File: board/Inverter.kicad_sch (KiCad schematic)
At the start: 19 parts, among them IC2 TLI4971A075T5UE0001XUMA1, Q1 IGC033S101, Q10 IGC033S101, Q11 IGC033S101, Q12 IGC033S101, Q2 IGC033S101, Q3 IGC033S101, Q4 IGC033S101, Q5 IGC033S101, Q6 IGC033S101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

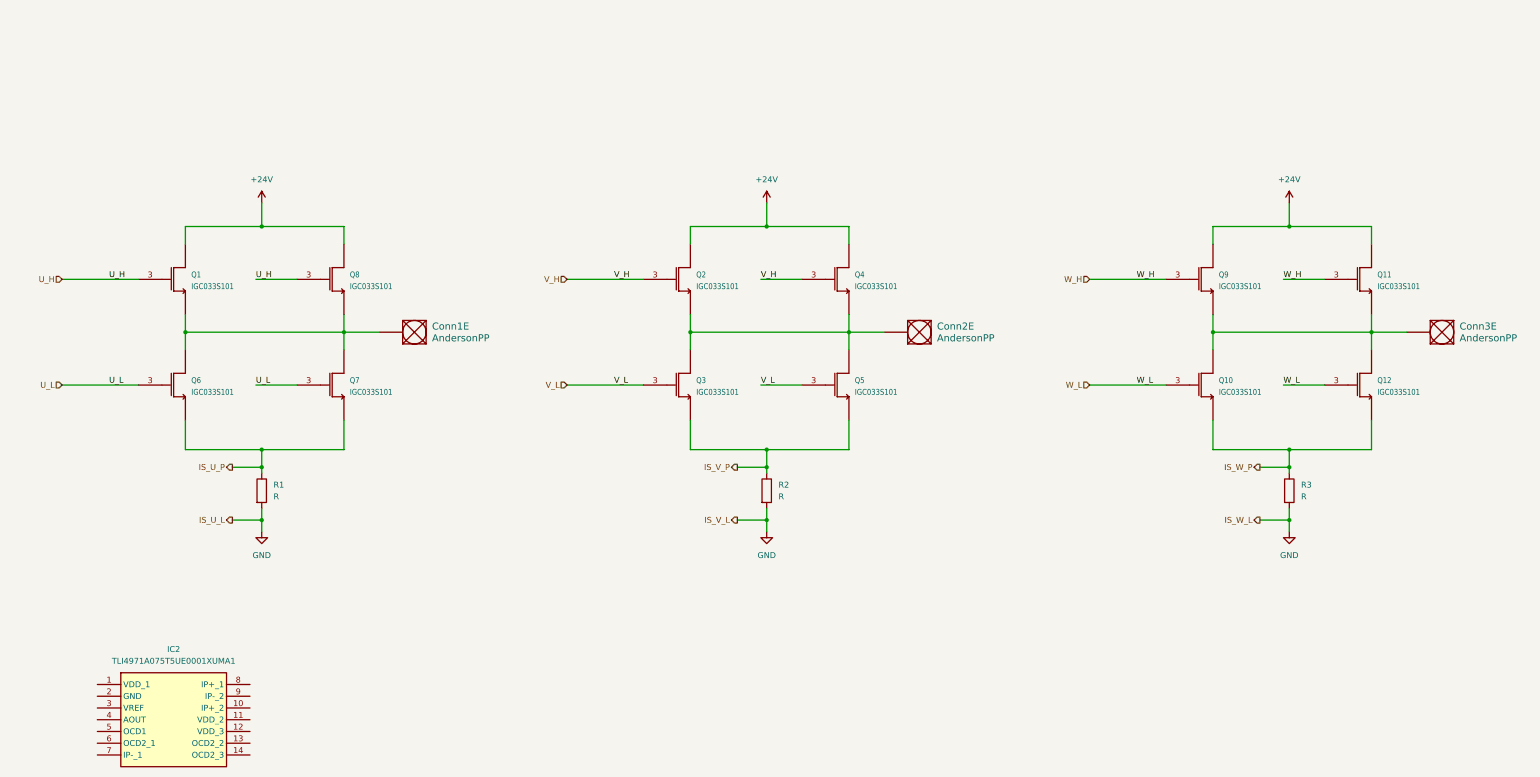
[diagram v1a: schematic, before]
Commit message: Added MCU and initial half bridge circuits from application circuit.
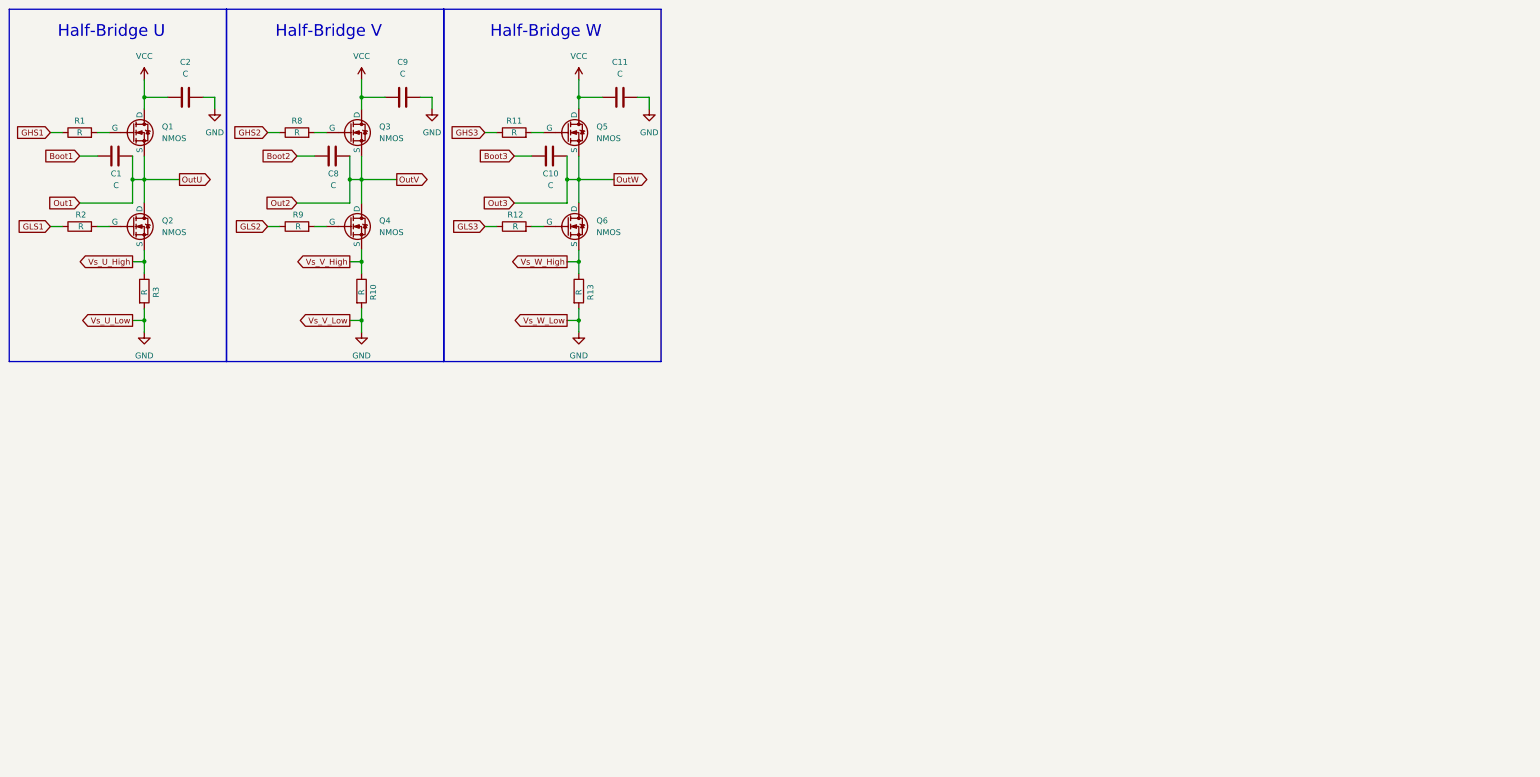
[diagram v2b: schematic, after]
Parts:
- removed Conn1, Conn2, Conn3: AndersonPP, MRDT_Connectors:Square_Anderson_1_H, symbol MRDT_Connectors:AndersonPP
- removed IC2: TLI4971A075T5UE0001XUMA1, brushless_moco_footprints:TLI4971A075T5UE0001XUMA1, symbol brushless_moco_symbols:TLI4971A075T5UE0001XUMA1
- removed Q1, Q10, Q11, Q12, Q2, Q3, Q4, Q5, Q6, Q7, Q8, Q9: IGC033S101, brushless_moco_footprints:IFX-PG-VSON-6-3-V, symbol brushless_moco_symbols:IGC033S101
- added C1, C10, C11, C2, C8, C9: C, symbol Device:C
- added Q1, Q2, Q3, Q4, Q5, Q6: NMOS, symbol Simulation_SPICE:NMOS
- added R10, R11, R12, R13, R8, R9: R, symbol Device:R
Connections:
- net GND: now also C11.2, C2.2, C9.2, R10.2, R13.2; no longer R1.2, R2.2
- net IS_U_P renamed GHS1
- net IS_V_P renamed GLS1
- net IS_W_P renamed Vs_U_High
- net Vs_U_High: now also Q2.3 (S)
- new net: Q5.2 (G), R11.2
- new net: Q6.2 (G), R12.2
- new net: Q4.2 (G), R9.2
- new net: Q2.2 (G), R2.2
- new net: Q1.2 (G), R1.2
- new net: Q3.2 (G), R8.2
- new net Boot1: C1.1
- new net Boot2: C8.1
- new net Boot3: C10.1
- new net GHS2: R8.1
- new net GHS3: R11.1
- new net GLS2: R9.1
- new net GLS3: R12.1
- new net Out1: C1.2, Q1.3 (S), Q2.1 (D)
- new net Out2: C8.2, Q3.3 (S), Q4.1 (D)
- new net Out3: C10.2, Q5.3 (S), Q6.1 (D)
- new net VCC: C11.1, C2.1, C9.1, Q1.1 (D), Q3.1 (D), Q5.1 (D)
- new net Vs_V_High: Q4.3 (S), R10.1
- new net Vs_W_High: Q6.3 (S), R13.1
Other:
- note added: "Half-Bridge U"
- note added: "Half-Bridge V"
- note added: "Half-Bridge W"
